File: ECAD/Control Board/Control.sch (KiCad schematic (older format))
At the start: 17 parts

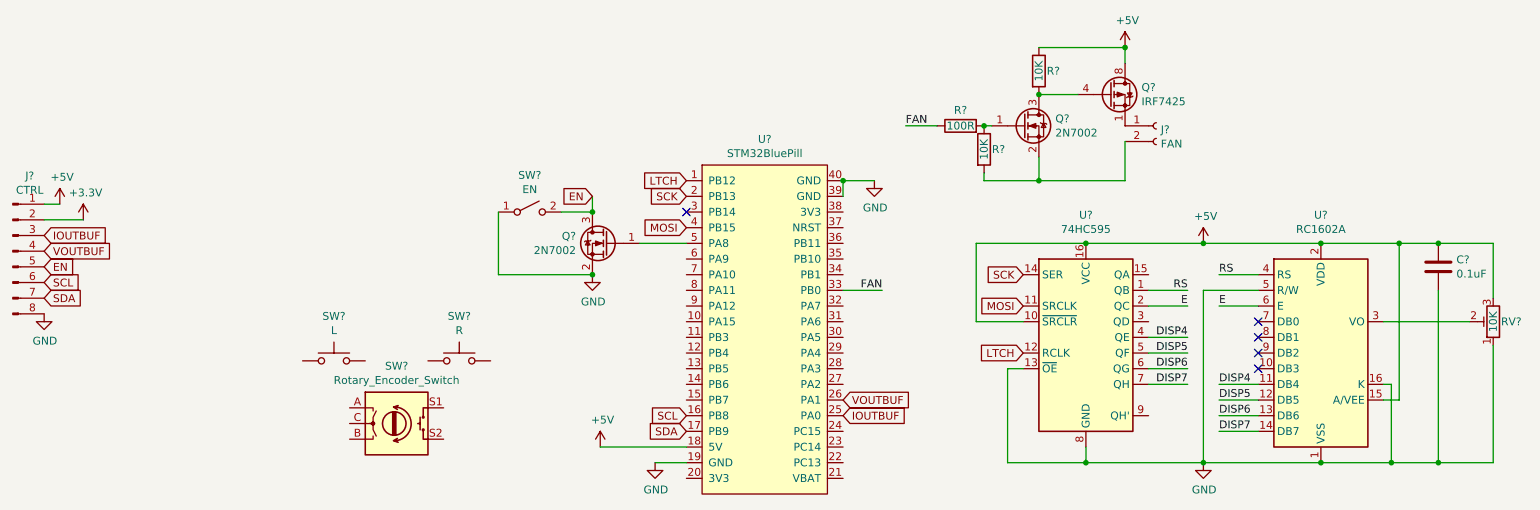
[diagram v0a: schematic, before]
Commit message: Add level shifter to control board
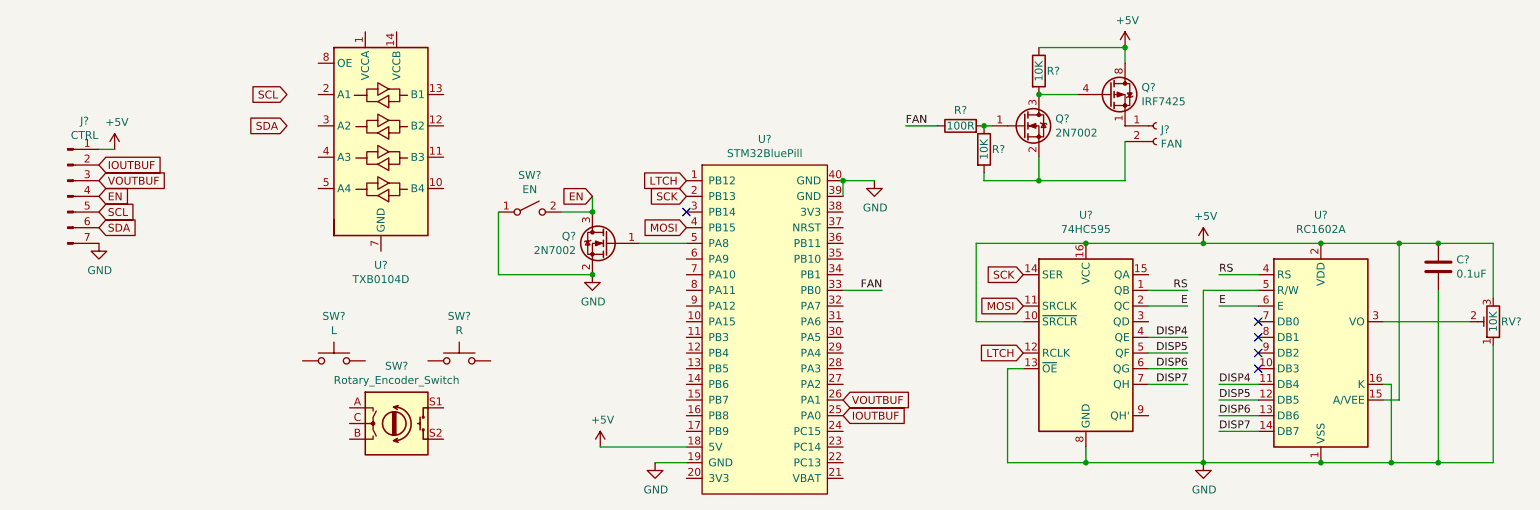
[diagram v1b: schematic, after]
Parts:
- removed J?: CTRL, symbol Connector:Conn_01x08_Male
- added J?: CTRL, symbol Connector:Conn_01x07_Male
- added U?: TXB0104D, Package_SO:SOIC-14_3.9x8.7mm_P1.27mm, symbol Logic_LevelTranslator:TXB0104D
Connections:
- net +5V: now also J?.1 (Pin_1)
- net EN: now also J?.4 (Pin_4)
- net GND: now also J?.7 (Pin_7)
- net IOUTBUF: now also J?.2 (Pin_2)
- net SCL: now also J?.5 (Pin_5); no longer U?.16 (PB8)
- net SDA: now also J?.6 (Pin_6); no longer U?.17 (PB9)
- net VOUTBUF: now also J?.3 (Pin_3)
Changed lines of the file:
@@
 L power:+5V #PWR?
 U 1 1 62054280
-P 1300 2450
-F 0 "#PWR?" H 1300 2300 50  0001 C CNN
-F 1 "+5V" H 1315 2623 50  0000 C CNN
-F 2 "" H 1300 2450 50  0001 C CNN
-F 3 "" H 1300 2450 50  0001 C CNN
-	1    1300 2450
-	1    0    0    -1
-$EndComp
-$Comp
-L power:+3.3V #PWR?
-U 1 1 62054B41
-P 1450 2550
-F 0 "#PWR?" H 1450 2400 50  0001 C CNN
-F 1 "+3.3V" H 1465 2723 50  0000 C CNN
-F 2 "" H 1450 2550 50  0001 C CNN
-F 3 "" H 1450 2550 50  0001 C CNN
-	1    1450 2550
-	1    0    0    -1
-$EndComp
-Wire Wire Line
-	1300 2450 1200 2450
-Wire Wire Line
-	1200 2550 1450 2550
-Text GLabel 1200 2650 2    50   Input ~ 0
+P 1650 2100
+F 0 "#PWR?" H 1650 1950 50  0001 C CNN
+F 1 "+5V" H 1665 2273 50  0000 C CNN
+F 2 "" H 1650 2100 50  0001 C CNN
+F 3 "" H 1650 2100 50  0001 C CNN
+	1    1650 2100
+	1    0    0    -1
+$EndComp
+Wire Wire Line
+	1650 2100 1550 2100
+Text GLabel 1550 2200 2    50   Input ~ 0
 IOUTBUF
-Text GLabel 1200 2750 2    50   Input ~ 0
+Text GLabel 1550 2300 2    50   Input ~ 0
 VOUTBUF
-Text GLabel 1200 2850 2    50   Input ~ 0
+Text GLabel 1550 2400 2    50   Input ~ 0
 EN
 $Comp
 L power:GND #PWR?
 U 1 1 6205654B
-P 1200 3150
-F 0 "#PWR?" H 1200 2900 50  0001 C CNN
-F 1 "GND" H 1205 2977 50  0000 C CNN
-F 2 "" H 1200 3150 50  0001 C CNN
-F 3 "" H 1200 3150 50  0001 C CNN
-	1    1200 3150
+P 1550 2700
+F 0 "#PWR?" H 1550 2450 50  0001 C CNN
+F 1 "GND" H 1555 2527 50  0000 C CNN
+F 2 "" H 1550 2700 50  0001 C CNN
+F 3 "" H 1550 2700 50  0001 C CNN
+	1    1550 2700
 	1    0    0    -1
 $EndComp
@@
 	1    0    0    -1
 $EndComp
-Text GLabel 1200 2950 2    50   Input ~ 0
+Text GLabel 1550 2500 2    50   Input ~ 0
 SCL
-Text GLabel 1200 3050 2    50   Input ~ 0
+Text GLabel 1550 2600 2    50   Input ~ 0
 SDA
-Text GLabel 5300 3800 0    50   Input ~ 0
+Text GLabel 2750 1750 0    50   Input ~ 0
 SCL
-Text GLabel 5300 3900 0    50   Input ~ 0
+Text GLabel 2750 1950 0    50   Input ~ 0
 SDA
 $Comp
-L Connector:Conn_01x08_Male J?
-U 1 1 6213E32B
-P 1000 2750
-F 0 "J?" H 1108 3231 50  0000 C CNN
-F 1 "CTRL" H 1108 3140 50  0000 C CNN
-F 2 "" H 1000 2750 50  0001 C CNN
-F 3 "~" H 1000 2750 50  0001 C CNN
-	1    1000 2750
-	1    0    0    -1
-$EndComp
+L Connector:Conn_01x07_Male J?
+U 1 1 62156A0D
+P 1350 2400
+F 0 "J?" H 1458 2881 50  0000 C CNN
+F 1 "CTRL" H 1458 2790 50  0000 C CNN
+F 2 "" H 1350 2400 50  0001 C CNN
+F 3 "~" H 1350 2400 50  0001 C CNN
+	1    1350 2400
+	1    0    0    -1
+$EndComp
+$Comp
+L Logic_LevelTranslator:TXB0104D U?
+U 1 1 6216022C
+P 3350 2050
+F 0 "U?" H 3350 1261 50  0000 C CNN
+F 1 "TXB0104D" H 3350 1170 50  0000 C CNN
+F 2 "Package_SO:SOIC-14_3.9x8.7mm_P1.27mm" H 3350 1300 50  0001 C CNN
+F 3 "http://www.ti.com/lit/ds/symlink/txb0104.pdf" H 3460 2145 50  0001 C CNN
+	1    3350 2050
+	1    0    0    -1
+$EndComp
